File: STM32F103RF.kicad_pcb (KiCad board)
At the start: 4 copper layers, 68 x 24 mm, 55 parts, among them J1 USB_C_Receptacle_USB2.0, J2 Conn_01x04, U1 SPX3819M5-L-3-3, U2 STM32F103C6Tx, U3 NRF24L01, Y1 16MHz, Y2 16MHz

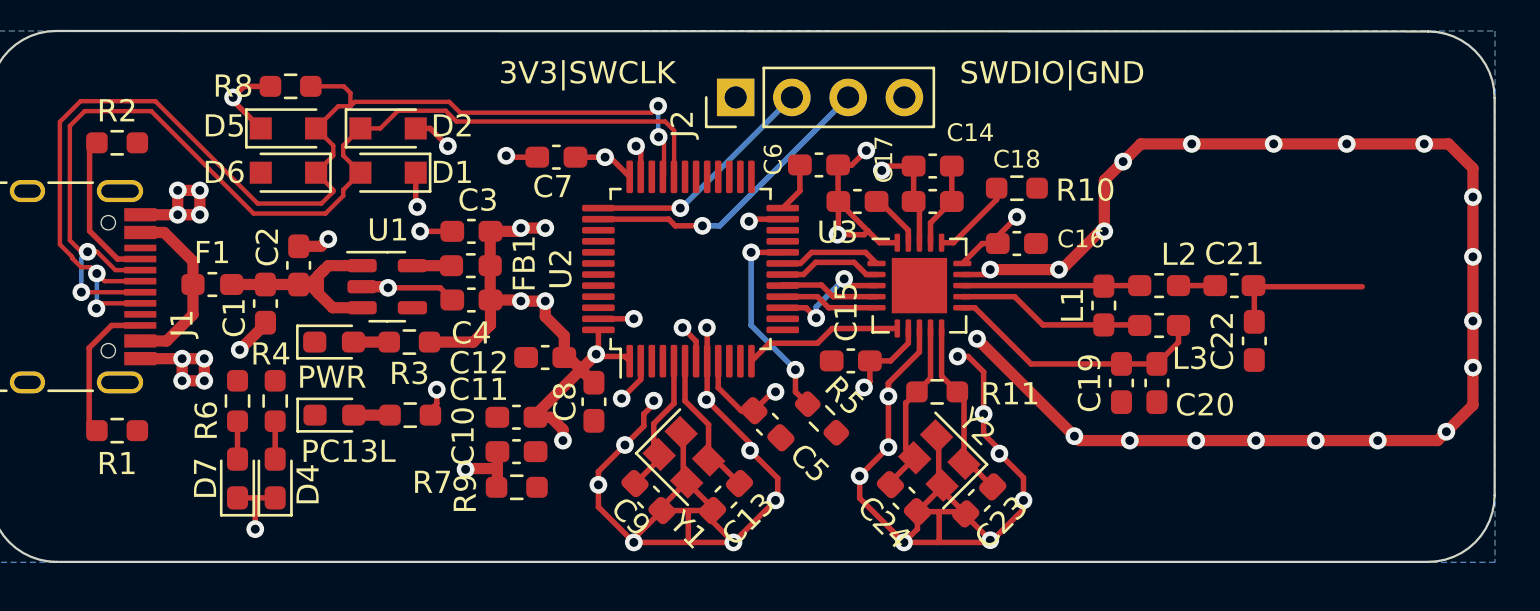
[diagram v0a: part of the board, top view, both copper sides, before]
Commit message: fixed footprints and added 3d models
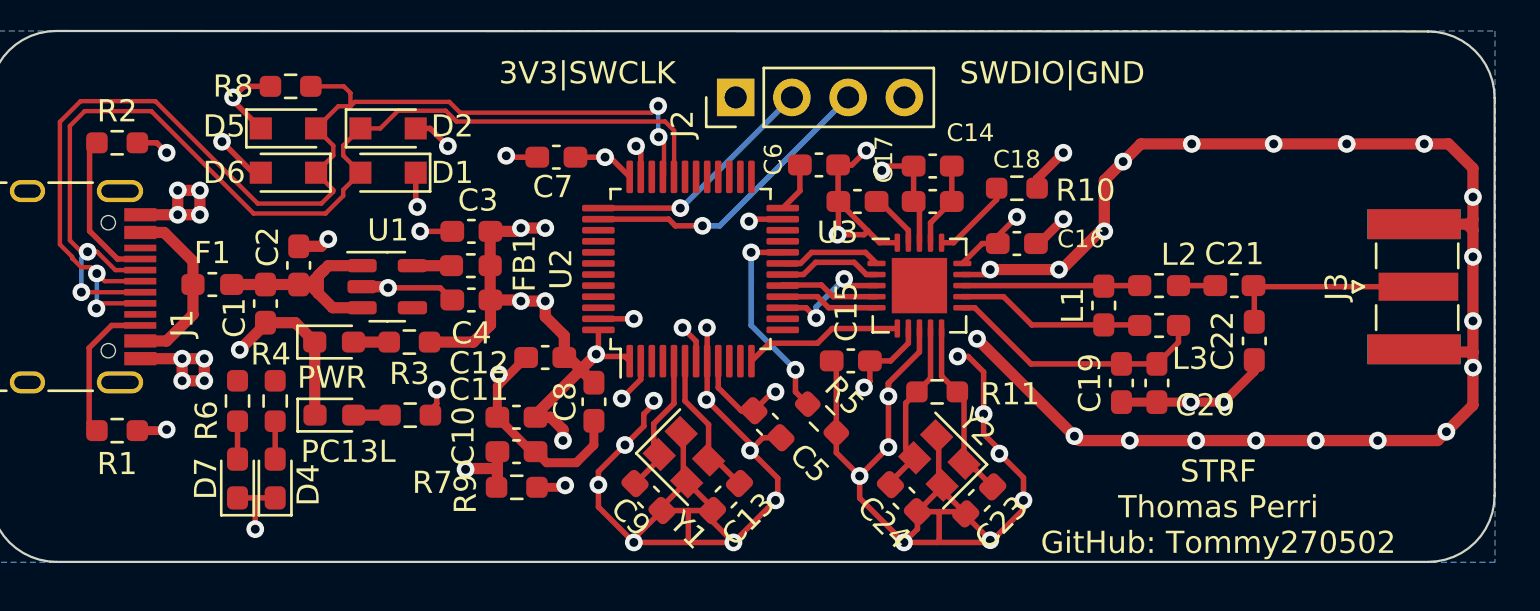
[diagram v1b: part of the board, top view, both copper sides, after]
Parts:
- added J3: Conn_Coaxial, Connector_Coaxial:SMA_Samtec_SMA-J-P-X-ST-EM1_EdgeMount, F.Cu at (100.3, 30.6)
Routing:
- net GND: track 185.1 -> 230.3 mm, vias 58 -> 66
- net Net-(C21-Pad2): track 6.59 -> 8.79 mm
- net 3.3V: track 53.5 -> 54.8 mm, vias 13 -> 14
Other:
- board text added: "STRF Thomas Perri GitHub: Tommy270502"

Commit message: added pictures and BOM
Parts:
- moved C2 44.9 mm to (81.2, 61.8)
- moved C20 44.9 mm to (120.0, 67.1)
- moved D4 44.9 mm to (80.2, 71.5)
- moved R4 44.9 mm to (80.2, 68.0)
- moved C11 44.9 mm to (91.1, 68.7)
- moved C14 44.9 mm to (109.9, 57.3)
- moved C15 44.9 mm to (106.2, 66.1)
- moved C18 44.9 mm to (109.9, 58.9)
- moved C19 44.9 mm to (118.4, 67.1)
- moved C21 44.9 mm to (123.5, 62.7)
- moved C24 44.9 mm to (108.6, 72.3)
- moved C4 44.9 mm to (89.0, 63.4)
- moved C5 44.9 mm to (102.4, 69.0)
- moved D1 44.9 mm to (85.3, 57.6)
- moved D2 44.9 mm to (85.3, 55.6)
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
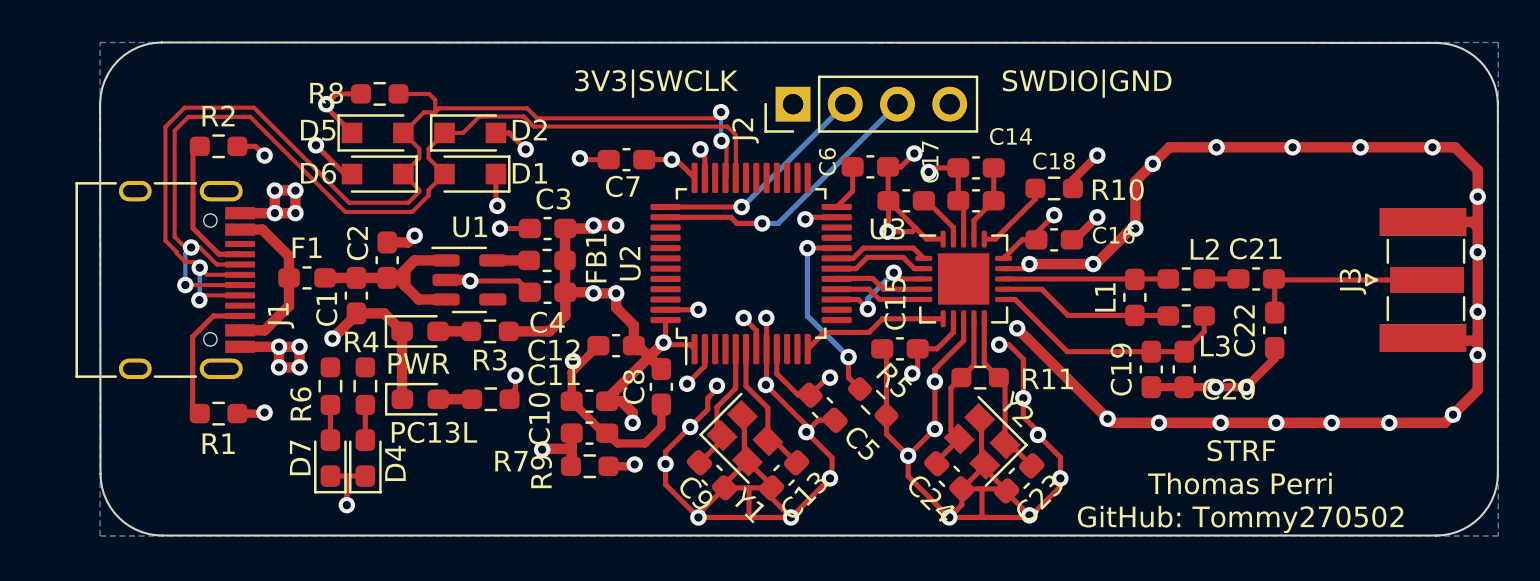
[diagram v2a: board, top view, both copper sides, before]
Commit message: shortened pcb by moving sma connector closer to the center
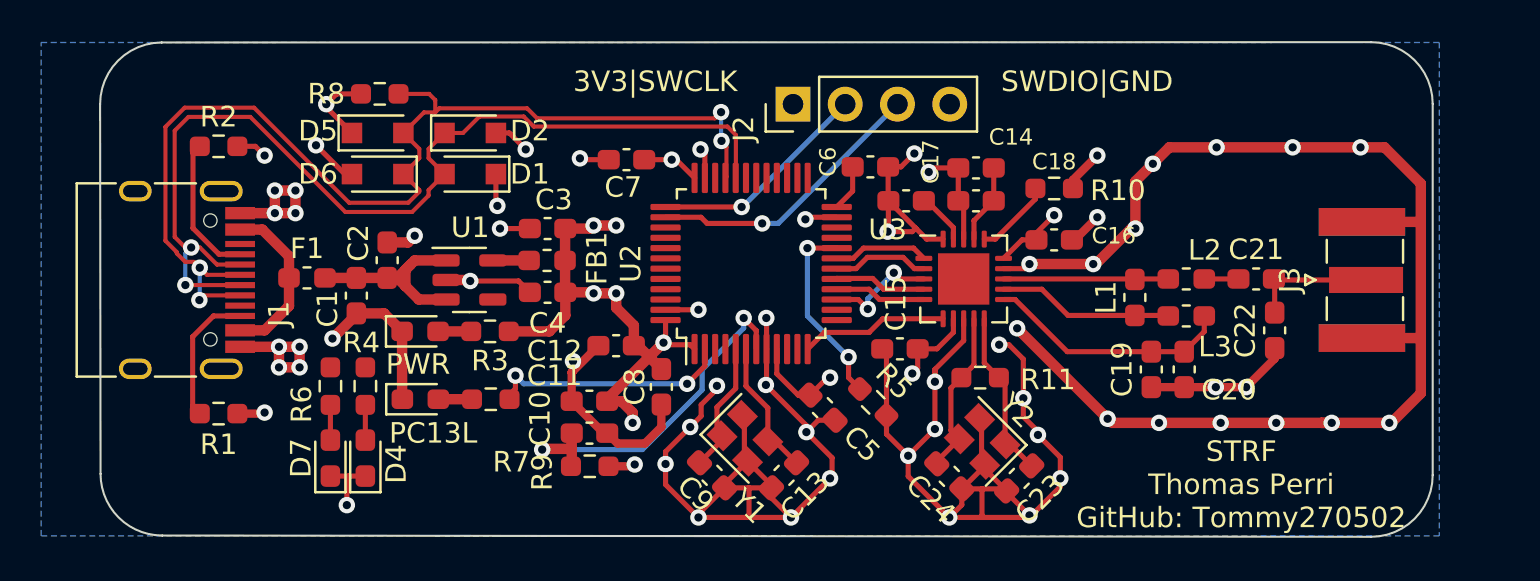
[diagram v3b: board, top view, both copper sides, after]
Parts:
- moved J3 2.97 mm to (128.6, 62.8)
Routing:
- net GND: track 230.3 -> 225.3 mm, vias 66 -> 60
- net Net-(C21-Pad2): track 8.79 -> 6.15 mm
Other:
- board size 68 x 24 mm -> 64.8 x 24.1 mm
